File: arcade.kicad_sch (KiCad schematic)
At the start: 0 parts

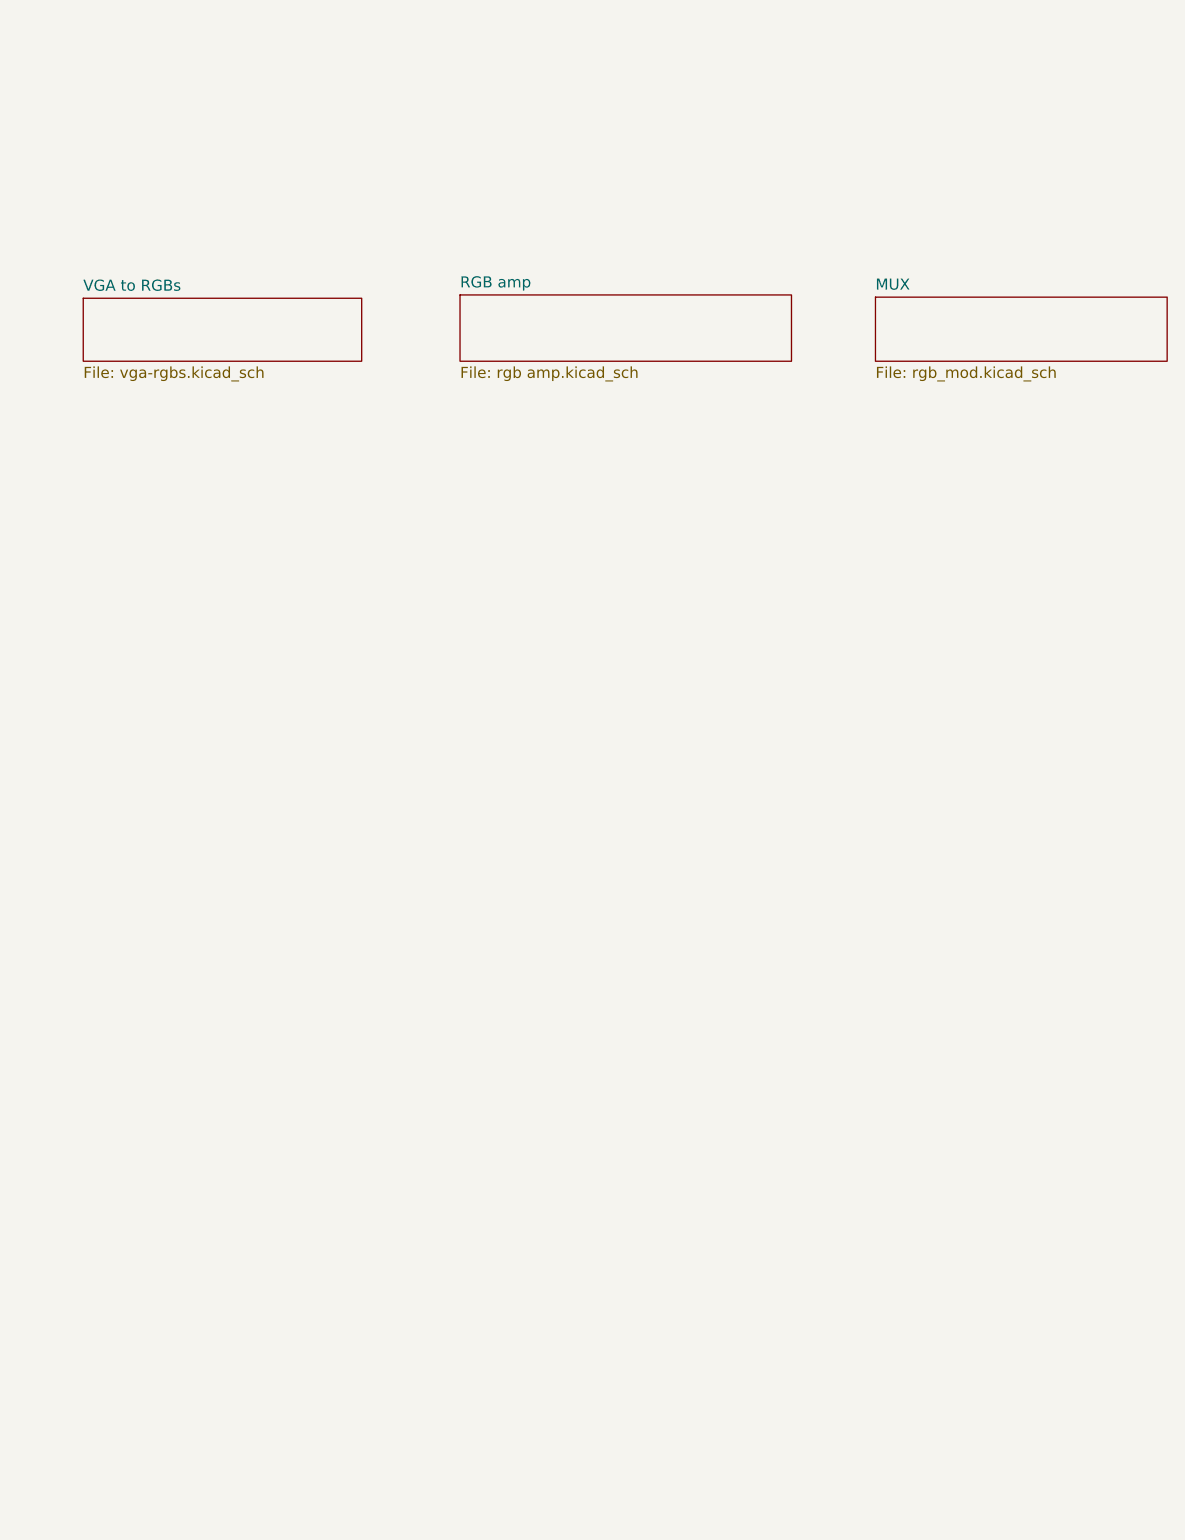
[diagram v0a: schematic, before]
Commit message: second design for nec tv and with inputs integrated
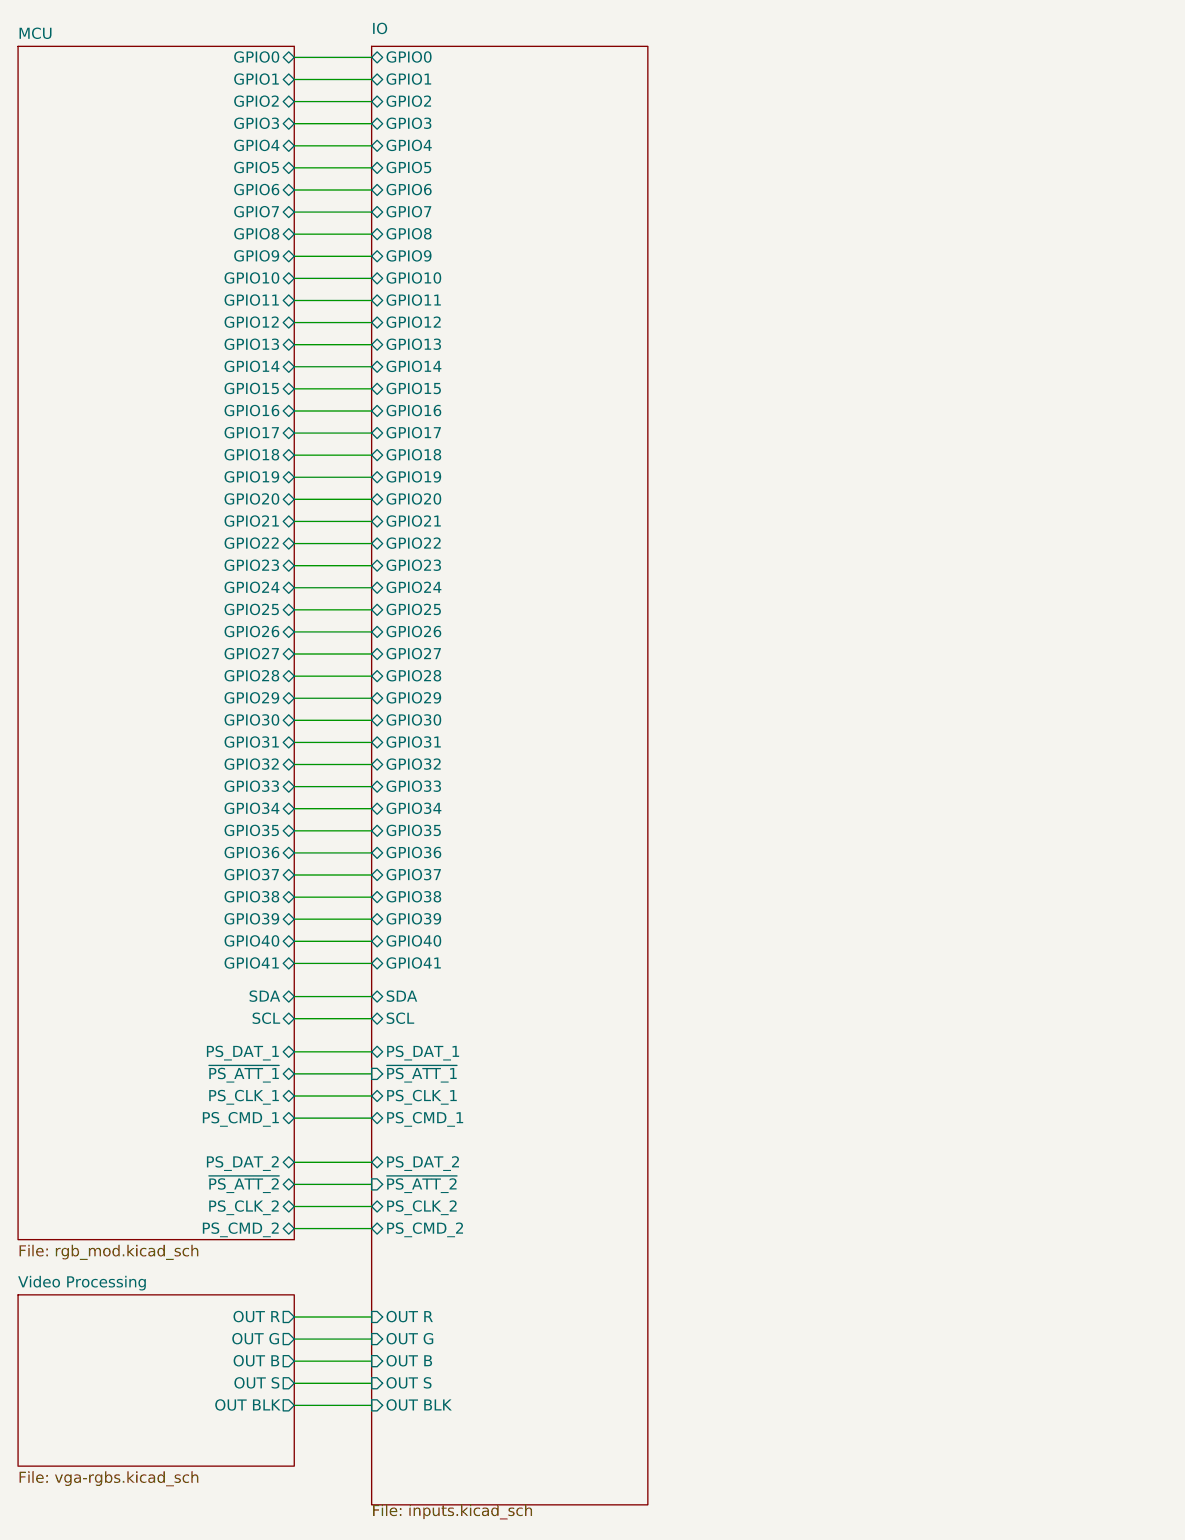
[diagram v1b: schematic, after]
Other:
- sheet MUX renamed MCU
- sheet VGA to RGBs renamed Video Processing
- removed sheet RGB amp
- added sheet IO (inputs.kicad_sch)
- sheet MCU ports: added GPIO0, GPIO1, GPIO10, GPIO11, GPIO12, GPIO13, GPIO14, GPIO15, GPIO16, GPIO17, GPIO18, GPIO19, GPIO2, GPIO20, GPIO21, GPIO22, GPIO23, GPIO24, GPIO25, GPIO26, GPIO27, GPIO28, GPIO29, GPIO3, GPIO30, GPIO31, GPIO32, GPIO33, GPIO34, GPIO35, GPIO36, GPIO37, GPIO38, GPIO39, GPIO4, GPIO40, GPIO41, GPIO5, GPIO6, GPIO7, GPIO8, GPIO9, PS_CLK_1, PS_CLK_2, PS_CMD_1, PS_CMD_2, PS_DAT_1, PS_DAT_2, SCL, SDA, ~{PS_ATT_1}, ~{PS_ATT_2}; removed none
- sheet Video Processing ports: added OUT B, OUT BLK, OUT G, OUT R, OUT S; removed none
